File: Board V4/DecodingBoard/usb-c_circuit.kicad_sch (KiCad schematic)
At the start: 5 parts, among them J1 UJ20-C-H-G-SMT-1-P16-TR, U3 USBLC6-2SC6

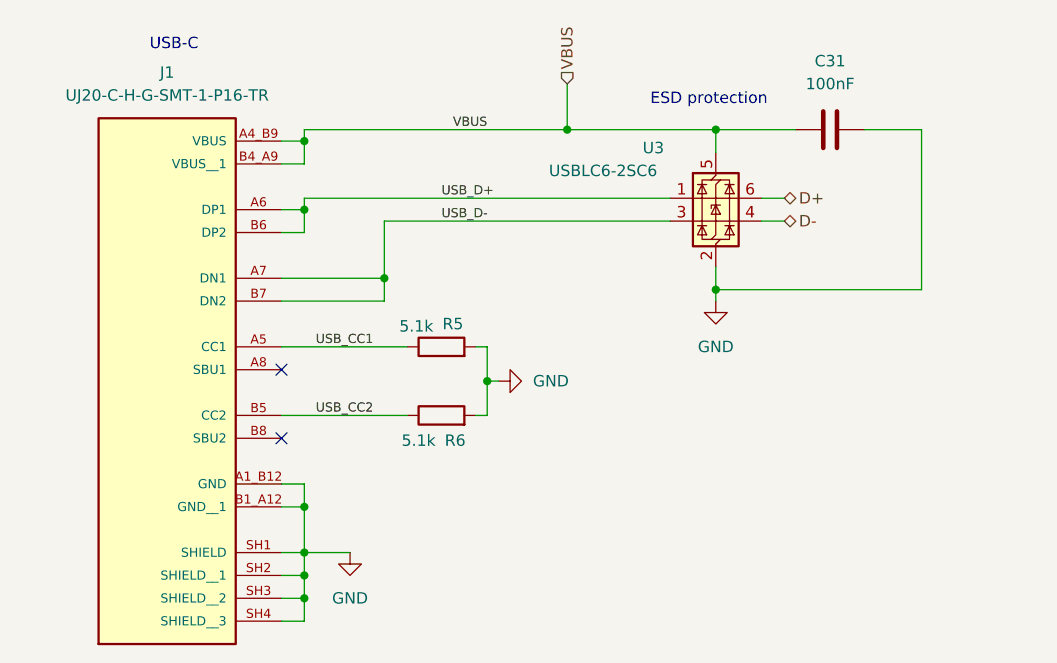
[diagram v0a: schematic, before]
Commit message: Changed USB-C symbol to match new connector
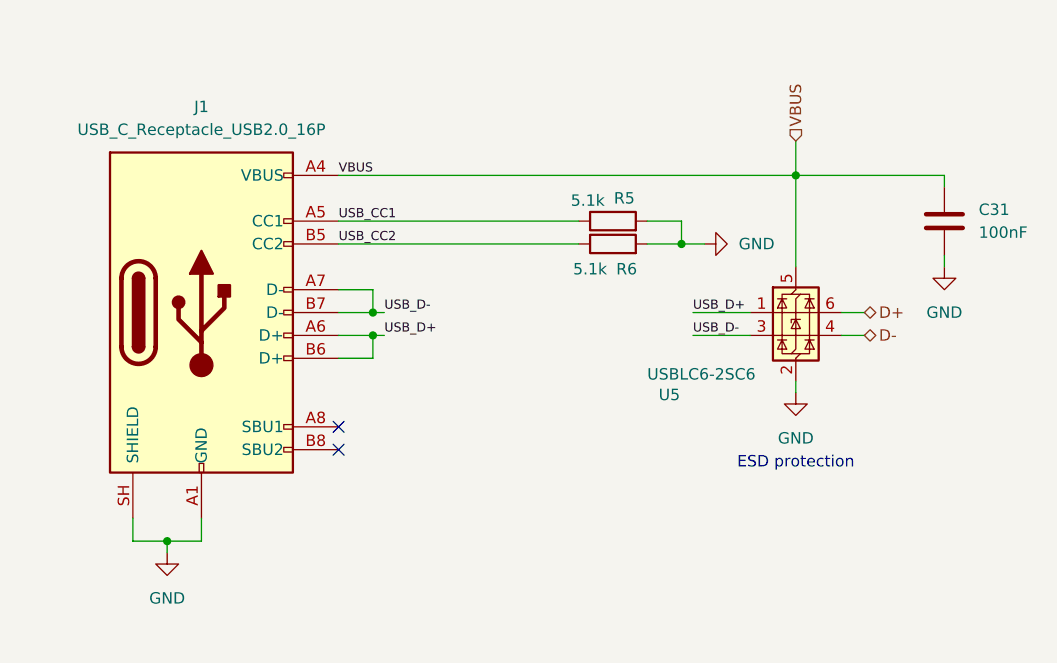
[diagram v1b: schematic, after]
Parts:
- removed J1: UJ20-C-H-G-SMT-1-P16-TR, Footprints:SAMESKY_UJ20-C-H-G-SMT-1-P16-TR, symbol UJ20-C-H-G-SMT-1-P16-TR:UJ20-C-H-G-SMT-1-P16-TR
- removed U3: USBLC6-2SC6, Package_TO_SOT_SMD:SOT-23-6, symbol Power_Protection:USBLC6-2SC6
- added J1: USB_C_Receptacle_USB2.0_16P, Connector_USB:USB_C_Receptacle_GCT_USB4110, symbol Connector:USB_C_Receptacle_USB2.0_16P
- added U5: USBLC6-2SC6, Package_TO_SOT_SMD:SOT-23-6, symbol Power_Protection:USBLC6-2SC6
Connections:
- net D+: now also U5.6 (I/O1)
- net D-: now also U5.4 (I/O2)
- net GND: now also J1.A1 (GND), J1.A12 (GND), J1.B1 (GND), J1.B12 (GND), J1.SH (SHIELD), U5.2 (GND)
- net USB_CC1: now also J1.A5 (CC1)
- net USB_CC2: now also J1.B5 (CC2)
- net USB_D+: now also J1.A6 (D+), J1.B6 (D+), U5.1 (I/O1)
- net USB_D-: now also J1.A7 (D-), J1.B7 (D-), U5.3 (I/O2)
- net VBUS: now also J1.A4 (VBUS), J1.A9 (VBUS), J1.B4 (VBUS), J1.B9 (VBUS), U5.5 (VBUS)
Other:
- note removed: "USB-C"

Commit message: Changed layout for new USB-C connector
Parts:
- renumbered U5 to U3
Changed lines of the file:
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@@
 		(in_pos_files yes)
 		(dnp no)
-		(property "Reference" "U5"
+		(property "Reference" "U3"
 			(at 88.9 59.944 0)
 			(show_name no)
@@
 			(project "DecodingBoard"
 				(path "/b438bce8-ca67-4245-91ae-f4475acc63f6/f85c4218-0aef-4639-a0dc-11a66bf7298f"
-					(reference "U5")
+					(reference "U3")
 					(unit 1)
 				)
